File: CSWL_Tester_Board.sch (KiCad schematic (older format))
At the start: 200 parts, among them J2 Conn_01x03, U1 CD74HC4067M, U2 CD74HC4067M, U3 MCP1700T-3302E_TT, U7 STM32F103C8Tx, Y1 8MHz

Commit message: Ruan: sperate to pin board and led board
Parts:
- removed J?: Conn_02x10_Counter_Clockwise, symbol Connector_Generic:Conn_02x10_Counter_Clockwise
- removed TP106: TP106, TestPoint:TestPoint_Loop_D2.54mm_Drill1.5mm_Beaded, symbol Connector:TestPoint
- removed TP107: TP107, TestPoint:TestPoint_Loop_D2.54mm_Drill1.5mm_Beaded, symbol Connector:TestPoint
- removed TP108: TP108, TestPoint:TestPoint_Loop_D2.54mm_Drill1.5mm_Beaded, symbol Connector:TestPoint
- removed TP109: TP109, TestPoint:TestPoint_Loop_D2.54mm_Drill1.5mm_Beaded, symbol Connector:TestPoint
- removed TP110: TP110, TestPoint:TestPoint_Loop_D2.54mm_Drill1.5mm_Beaded, symbol Connector:TestPoint
- removed TP111: TP111, TestPoint:TestPoint_Loop_D2.54mm_Drill1.5mm_Beaded, symbol Connector:TestPoint
- removed TP200: TP200, TestPoint:TestPoint_Loop_D2.54mm_Drill1.5mm_Beaded, symbol Connector:TestPoint
- removed TP201: TP201, TestPoint:TestPoint_Loop_D2.54mm_Drill1.5mm_Beaded, symbol Connector:TestPoint
- removed TP301: TP301, TestPoint:TestPoint_Loop_D2.54mm_Drill1.5mm_Beaded, symbol Connector:TestPoint
- removed TP302: TP302, TestPoint:TestPoint_Loop_D2.54mm_Drill1.5mm_Beaded, symbol Connector:TestPoint
- removed TP304: TP304, TestPoint:TestPoint_Loop_D2.54mm_Drill1.5mm_Beaded, symbol Connector:TestPoint
- removed TP305: TP305, TestPoint:TestPoint_Loop_D2.54mm_Drill1.5mm_Beaded, symbol Connector:TestPoint
- removed TP307: TP307, TestPoint:TestPoint_Loop_D2.54mm_Drill1.5mm_Beaded, symbol Connector:TestPoint
- removed TP308: TP308, TestPoint:TestPoint_Loop_D2.54mm_Drill1.5mm_Beaded, symbol Connector:TestPoint
- removed TP310: TP310, TestPoint:TestPoint_Loop_D2.54mm_Drill1.5mm_Beaded, symbol Connector:TestPoint
- removed TP311: TP311, TestPoint:TestPoint_Loop_D2.54mm_Drill1.5mm_Beaded, symbol Connector:TestPoint
- removed TP313: TP313, TestPoint:TestPoint_Loop_D2.54mm_Drill1.5mm_Beaded, symbol Connector:TestPoint
- removed TP314: TP314, TestPoint:TestPoint_Loop_D2.54mm_Drill1.5mm_Beaded, symbol Connector:TestPoint
- removed TP316: TP316, TestPoint:TestPoint_Loop_D2.54mm_Drill1.5mm_Beaded, symbol Connector:TestPoint
- removed TP317: TP317, TestPoint:TestPoint_Loop_D2.54mm_Drill1.5mm_Beaded, symbol Connector:TestPoint
- removed TP319: TP319, TestPoint:TestPoint_Loop_D2.54mm_Drill1.5mm_Beaded, symbol Connector:TestPoint
- removed TP320: TP320, TestPoint:TestPoint_Loop_D2.54mm_Drill1.5mm_Beaded, symbol Connector:TestPoint
- removed TP322: TP322, TestPoint:TestPoint_Loop_D2.54mm_Drill1.5mm_Beaded, symbol Connector:TestPoint
- removed TP323: TP323, TestPoint:TestPoint_Loop_D2.54mm_Drill1.5mm_Beaded, symbol Connector:TestPoint
- removed TP325: TP325, TestPoint:TestPoint_Loop_D2.54mm_Drill1.5mm_Beaded, symbol Connector:TestPoint
- removed TP326: TP326, TestPoint:TestPoint_Loop_D2.54mm_Drill1.5mm_Beaded, symbol Connector:TestPoint
- removed TP328: TP328, TestPoint:TestPoint_Loop_D2.54mm_Drill1.5mm_Beaded, symbol Connector:TestPoint
- removed TP329: TP329, TestPoint:TestPoint_Loop_D2.54mm_Drill1.5mm_Beaded, symbol Connector:TestPoint
- removed TP331: TP331, TestPoint:TestPoint_Loop_D2.54mm_Drill1.5mm_Beaded, symbol Connector:TestPoint
- removed TP332: TP332, TestPoint:TestPoint_Loop_D2.54mm_Drill1.5mm_Beaded, symbol Connector:TestPoint
- removed TP334: TP334, TestPoint:TestPoint_Loop_D2.54mm_Drill1.5mm_Beaded, symbol Connector:TestPoint
- removed TP335: TP335, TestPoint:TestPoint_Loop_D2.54mm_Drill1.5mm_Beaded, symbol Connector:TestPoint
- added J?: IDC 2.54mm, Connector_IDC:IDC-Header_2x10_P2.54mm_Vertical, symbol Connector_Generic:Conn_02x10_Odd_Even
- added J? (x2): Conn_02x10_Odd_Even, Connector_IDC:IDC-Header_2x10_P2.54mm_Vertical, symbol Connector_Generic:Conn_02x10_Odd_Even
- D?: value LED -> LED5
- D?: value LED2 -> LED6
- D?: value LED3 -> LED7
- D?: value LED4 -> LED8
- D?: value LED -> LED9
- D?: value LED2 -> LED10
- D?: value LED3 -> LED11
- D?: value LED4 -> LED12
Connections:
- wire segments 695 -> 732
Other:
- note added: "To Pin Board\n"

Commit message: Ruan: fix bug' '
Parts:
- removed R? (x6): 10K, Resistor_SMD:R_0603_1608Metric, symbol Device:R
- removed U? (x2): SN74HC151DR, Package_SO:SOIC-16_3.9x9.9mm_P1.27mm, symbol 74xx:74LS151
- added R91, R92, R93, R94, R95, R96: 10K, Resistor_SMD:R_0603_1608Metric, symbol Device:R
- added U26, U28: SN74HC151DR, symbol 74xx:74LS151
- gave numbers to parts that had none: 143
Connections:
- net labels removed: LED7-8_Output
- wire segments 732 -> 716
- no-connect marks 6 -> 29

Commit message: Ruan: fix 2
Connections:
- wire segments 716 -> 717

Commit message: Ruan: fix 3
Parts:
- D1, D10, D11, D12, D2, D3, D4, D5, D6, D7, D8, D9: footprint (none) -> LED_SMD:LED_0603_1608Metric
- U26, U28: footprint (none) -> Package_SO:SOIC-16_3.9x9.9mm_P1.27mm
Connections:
- net labels added: LED_1-6_S0, LED_1-6_S1, LED_1-6_S2, LED_7-12_S0, LED_7-12_S1, LED_7-12_S2
- wire segments 717 -> 725
- no-connect marks 29 -> 23
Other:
- note added: "Option ( one way : 3.3V_A with 3.3V_B )"
- note added: "Option ( tow way : 3.3V_A , 3.3V_B )"
- moved on the sheet: R91, R92, R93, R94, R95, R96

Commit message: Ruan: make pcb V0
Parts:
- added C25: 0.1uF, Capacitor_SMD:C_0603_1608Metric, symbol Device:C
- added Q6, Q7, Q8, Q9: 2N7002LT1G, digikey-footprints:SOT-23-3, symbol dk_Transistors-FETs-MOSFETs-Single:2N7002LT1G
- added R100, R104: 0R(NC), Resistor_SMD:R_0603_1608Metric, symbol Device:R
- added R101, R105, R97: 33R, Resistor_SMD:R_0603_1608Metric, symbol Device:R
- added R102, R106, R98: 100K, Resistor_SMD:R_0603_1608Metric, symbol Device:R
- added R103, R107, R108, R109, R110, R117, R118, R99: 10K, Resistor_SMD:R_0603_1608Metric, symbol Device:R
- added R111, R112, R113, R114, R115, R116, R119, R120, R121, R122, R123, R124: 0R, Resistor_SMD:R_0603_1608Metric, symbol Device:R
- added U29: 74HC4016, Package_SO:TSSOP-14_4.4x5mm_P0.65mm, symbol RuanProject:74HC4016
- R46, R60: value 10K -> 0R(NC)
- R47: value 10K -> 33R
- R48: value 10K -> 100K
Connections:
- net labels added: AS4_Y, AS4_Z, CSWL_TestMode_S2, CSWL_TestMode_S3, CSWL_TestMode_S4, CSWL_TestMode_SN, GNDA, TP300, TP303, TP306, TPXXX, TestMode_S2, TestMode_S3, TestMode_S4, TestMode_SN
- wire segments 725 -> 829
- no-connect marks 23 -> 15
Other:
- moved on the sheet: C1, C2, Q1, Q2, Q3, Q4, Q5, R1, R11, R12, R19, R2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

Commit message: Ruan: start PCB design
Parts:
- removed Y1: 8MHz, Crystal:Crystal_SMD_3225-4Pin_3.2x2.5mm_HandSoldering, symbol Device:Crystal
- added R125: 33R, Resistor_SMD:R_0603_1608Metric, symbol Device:R
- added R126, R127, R128, R129, R130: 0R(NC), Resistor_SMD:R_0603_1608Metric, symbol Device:R
- added Y1: Crystal_GND24, RuanProject:Crystal_SMD_3225-4Pin_3.2x2.5mm_HandSoldering, symbol Device:Crystal_GND24
- C11, C12: value 20pF -> 22pF
- R13, R14, R15, R16, R17, R18, R25, R26, R27, R28, R29, R30: value 10K -> 680R
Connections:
- wire segments 829 -> 862

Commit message: Ruan： PCB designing
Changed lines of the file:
@@
 Wire Wire Line
 	7100 2890 6690 2890
-Text Label 19840 3550 2    50   ~ 0
+Text Label 19410 3450 0    50   ~ 0
 Serial_nEN
-Text Label 19860 3650 2    50   ~ 0
+Text Label 19420 3550 0    50   ~ 0
 Shift_reg_lock
 Text Label 19800 3750 2    50   ~ 0
 Shift_reg_clear
-Text Label 19790 3350 2    50   ~ 0
+Text Label 19420 3640 0    50   ~ 0
 Serial_CLK
-Text Label 19810 3450 2    50   ~ 0
+Text Label 19400 3350 0    50   ~ 0
 Serial_Input
 Text Label 5350 1990 0    50   ~ 0

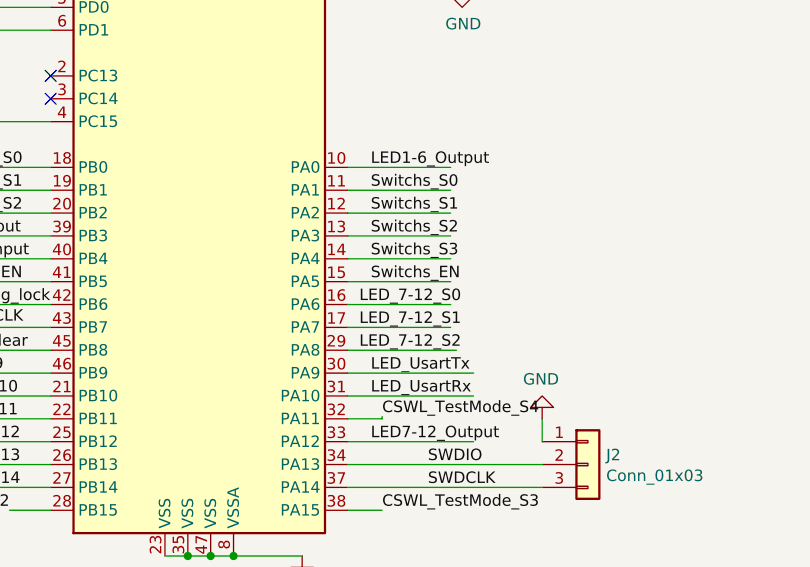
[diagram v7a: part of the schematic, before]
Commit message: Ruan: PCB design -> base layout finish
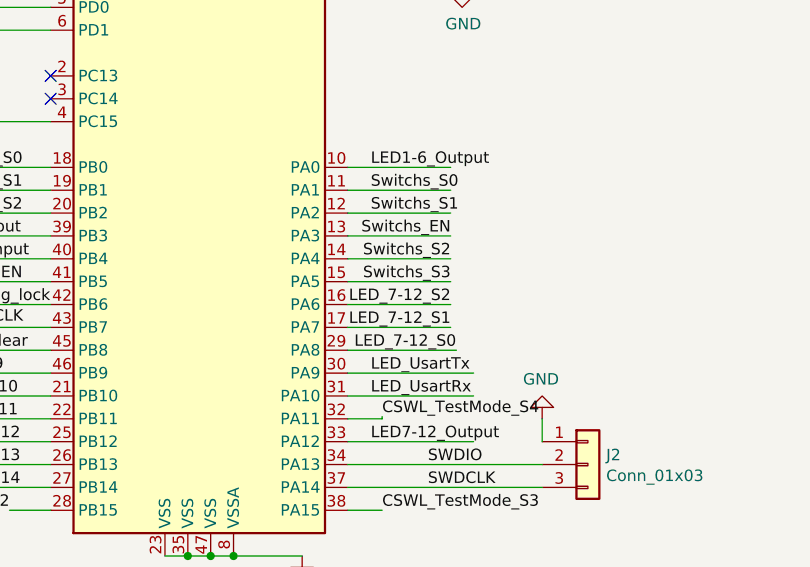
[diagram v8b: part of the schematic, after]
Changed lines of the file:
@@
 Text Label 21300 3150 0    50   ~ 0
 Switchs_S1
-Text Label 21300 3250 0    50   ~ 0
+Text Label 21650 3350 2    50   ~ 0
 Switchs_S2
-Text Label 21300 3350 0    50   ~ 0
+Text Label 21650 3450 2    50   ~ 0
 Switchs_S3
 Wire Wire Line
@@
 Text Label 11558 1400 0    50   ~ 0
 LED1_OUT
-Text Label 21300 3450 0    50   ~ 0
+Text Label 21650 3250 2    50   ~ 0
 Switchs_EN
 Text Label 21300 2950 0    50   ~ 0
@@
 Wire Wire Line
 	21200 3750 21675 3750
-Text Label 21250 3550 0    50   ~ 0
+Text Label 21674 3750 2    50   ~ 0
 LED_7-12_S0
-Text Label 21250 3650 0    50   ~ 0
-LED_7-12_S1
-Text Label 21250 3750 0    50   ~ 0
-LED_7-12_S2
 Text Label 20550 9000 0    50   ~ 0
 LED_7-12_S0
@@
 Wire Wire Line
 	17360 12420 17360 12320
+Text Label 21650 3650 2    50   ~ 0
+LED_7-12_S1
+Text Label 21650 3550 2    50   ~ 0
+LED_7-12_S2
 $EndSCHEMATC
